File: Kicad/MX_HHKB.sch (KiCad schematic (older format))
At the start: 149 parts, among them J1 USB_mini_micro_B, K1 K00, K10 K09, K11 K0A, K12 K0B, K13 K0C, K14 K10, K15 K11, K16 K12, K17 K13, K18 K14, K19 K15, K2 K01, K20 K16, K21 K17, K22 K18, K23 K19, K24 K1A, K25 K1B, K26 K1C, K27 K20, K28 K21, K29 K22, K3 K02, K30 K23, K31 K24, K32 K25, K33 K26, K34 K27, K35 K28, K36 K29, K37 K2A, K38 K2B, K39 K2C, K4 K03, K40 K30, K41 K31, K42 K32, K43 K33, K44 K34, K45 K35, K46 K36, K47 K37, K48 K38, K49 K39, K5 K04, K50 K3A, K51 K3B, K52 K3C, K53 K41, K54 K42, K55 K45, K56 K48, K57 K49, K58 K4A, K59 K4B, K6 K05, K60 K4C, K61 Ctrl, K62 L_ALT, K63 SPACE, K64 SPACE, K65 R_ALT, K66 R_ALT, K67 R_GUI, K68 R_GUI, K7 K06, K8 K07, K9 K08, SW1 SW_PUSH, U0 ATMEGA32U4, X1 XTAL_GND

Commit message: - Replaced all Diodes with SMD
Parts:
- D1, D10, D11, D12, D13, D14, D15, D16, D17, D18, D19, D2, D20, D21, D22, D23, D24, D25, D26, D27, D28, D29, D3, D30, D31, D32, D33, D34, D35, D36, D37, D38, D39, D4, D40, D41, D42, D43, D44, D45, D46, D47, D48, D49, D5, D50, D51, D52, D53, D54, D55, D56, D57, D58, D59, D6, D60, D7, D8, D9: footprint Footprint:D_SOD123_axial -> Footprint:D_SOD123

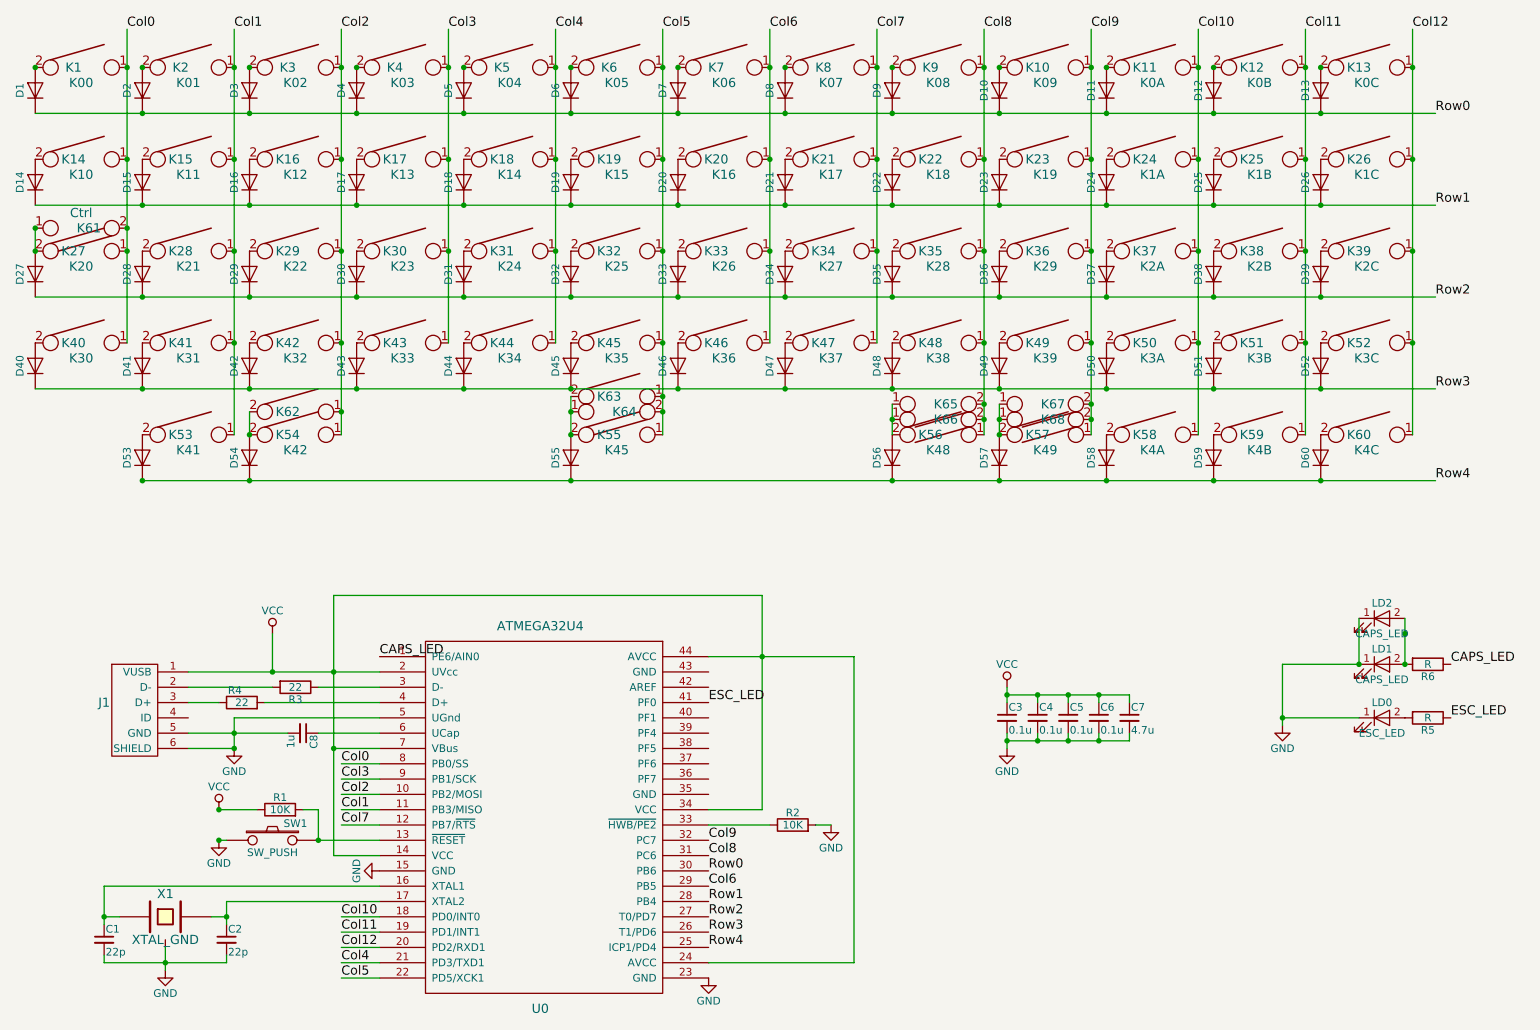
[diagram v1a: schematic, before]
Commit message: - Routing, again and again - Naming all Diodes - Fixed some bugs for holes - Added holes for PCB stabilizers
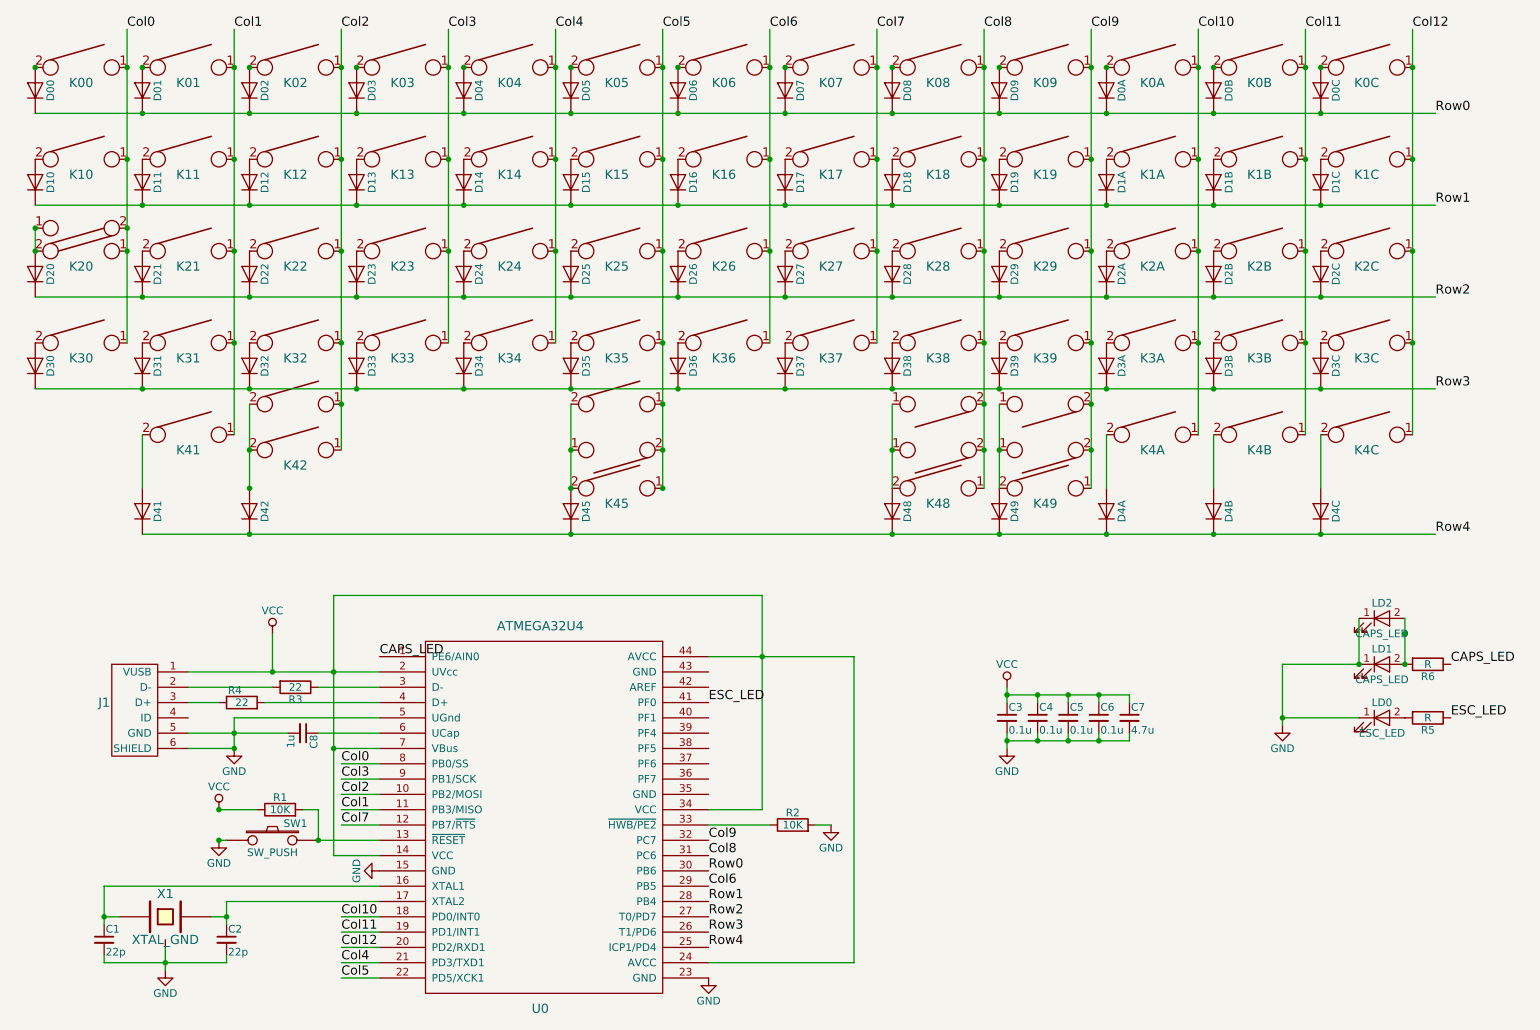
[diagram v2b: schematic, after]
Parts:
- D1: value D -> D00
- D10: value D -> D09
- D11: value D -> D0A
- D12: value D -> D0B
- D13: value D -> D0C
- D14: value D -> D10
- D15: value D -> D11
- D16: value D -> D12
- D17: value D -> D13
- D18: value D -> D14
- D19: value D -> D15
- D2: value D -> D01
- D20: value D -> D16
- D21: value D -> D17
- D22: value D -> D18
- D23: value D -> D19
- D24: value D -> D1A
- D25: value D -> D1B
- D26: value D -> D1C
- D27: value D -> D20
- D28: value D -> D21
- D29: value D -> D22
- D3: value D -> D02
- D30: value D -> D23
- D31: value D -> D24
- D32: value D -> D25
- D33: value D -> D26
- D34: value D -> D27
- D35: value D -> D28
- D36: value D -> D29
- D37: value D -> D2A
- D38: value D -> D2B
- D39: value D -> D2C
- D4: value D -> D03
- D40: value D -> D30
- D41: value D -> D31
- D42: value D -> D32
- D43: value D -> D33
- D44: value D -> D34
- D45: value D -> D35
- D46: value D -> D36
- D47: value D -> D37
- D48: value D -> D38
- D49: value D -> D39
- D5: value D -> D04
- D50: value D -> D3A
- D51: value D -> D3B
- D52: value D -> D3C
- D53: value D -> D41
- D54: value D -> D42
- D55: value D -> D45
- D56: value D -> D48
- D57: value D -> D49
- D58: value D -> D4A
- D59: value D -> D4B
- D6: value D -> D05
- D60: value D -> D4C
- D7: value D -> D06
- D8: value D -> D07
- D9: value D -> D08

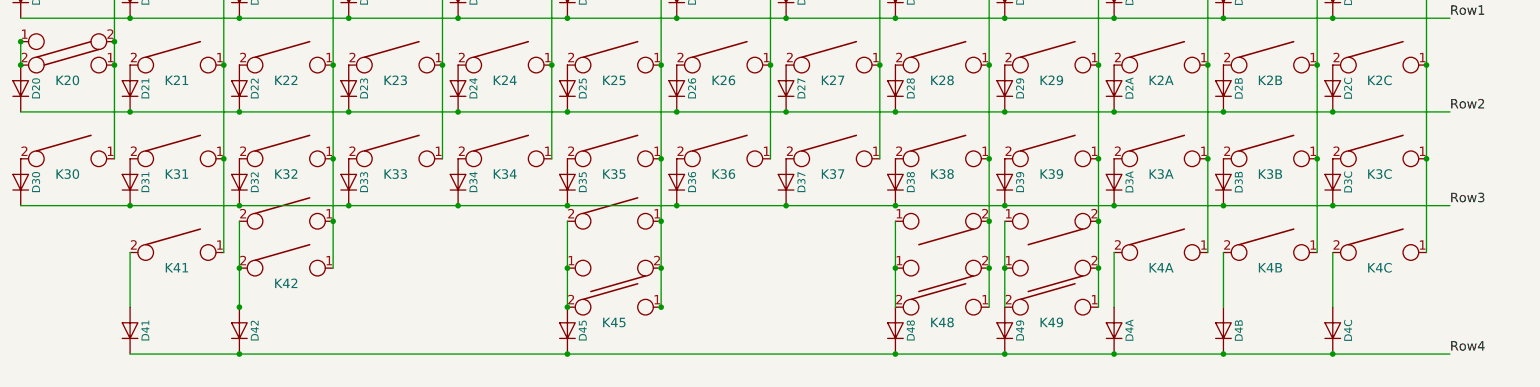
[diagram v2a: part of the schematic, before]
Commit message: - Updated plate.dxf (now use layers to simulate all available layouts) - Added revert 6u spacebar
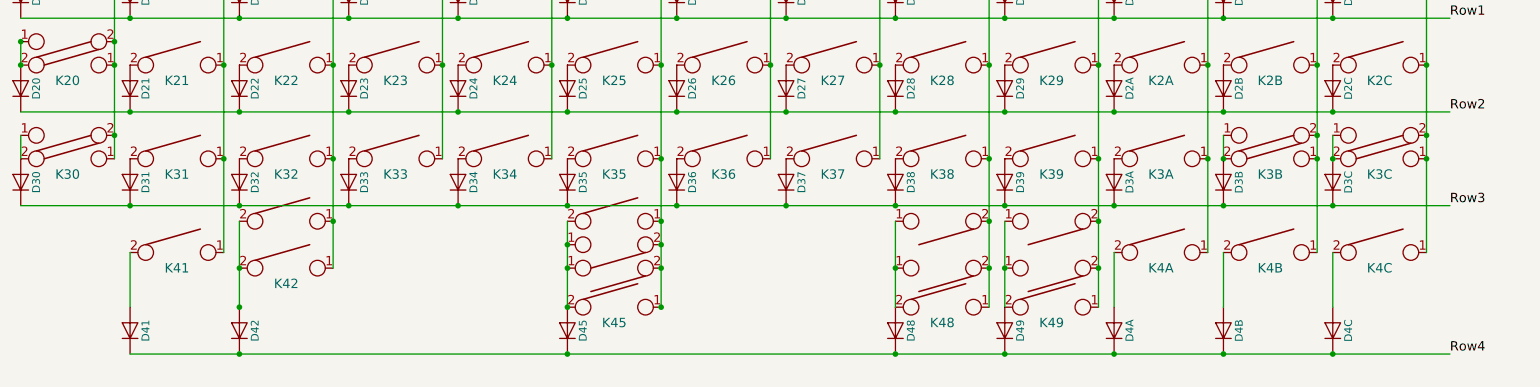
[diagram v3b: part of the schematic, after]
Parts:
- added K69: K30, Footprint:Mx_Alps_225, symbol KEYSW
- added K70: K3C, Footprint:Mx_Alps_100, symbol KEYSW
- added K71: K3B, Footprint:Mx_Alps_175, symbol KEYSW
- added K72: SPACE, Footprint:Mx_Alps_100, symbol KEYSW
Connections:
- net Col0: now also K69.2
- net Col11: now also K71.2
- net Col12: now also K70.2
- net Col5: now also K72.2
- net at D55.2 (A), K55.2, K63.2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: now also K72.1
- net at D40.2 (A), K40.2: now also K69.1
- net at D51.2 (A), K51.2: now also K71.1
- net at D52.2 (A), K52.2: now also K70.1
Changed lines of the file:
@@
 Connection ~ 2150 4150
 Connection ~ 4250 4150
+$Comp
+L KEYSW K69
+U 1 1 591EE9FF
+P 1050 2750
+F 0 "K69" H 1000 2750 60  0001 C CNN
+F 1 "K30" H 1050 2650 60  0001 C CNN
+F 2 "Footprint:Mx_Alps_225" H 1050 2750 60  0001 C CNN
+F 3 "" H 1050 2750 60  0000 C CNN
+	1    1050 2750
+	-1   0    0    1
+$EndComp
+Wire Wire Line
+	750  2750 750  2900
+Connection ~ 1350 2750
+$Comp
+L KEYSW K70
+U 1 1 59228C81
+P 9450 2750
+F 0 "K70" H 9400 2750 60  0001 C CNN
+F 1 "K3C" H 9450 2650 60  0001 C CNN
+F 2 "Footprint:Mx_Alps_100" H 9450 2750 60  0001 C CNN
+F 3 "" H 9450 2750 60  0000 C CNN
+	1    9450 2750
+	-1   0    0    1
+$EndComp
+Wire Wire Line
+	9150 2750 9150 2900
+Connection ~ 9150 2900
+Connection ~ 9750 2750
+$Comp
+L KEYSW K71
+U 1 1 59228EDE
+P 8750 2750
+F 0 "K71" H 8700 2750 60  0001 C CNN
+F 1 "K3B" H 8750 2650 60  0001 C CNN
+F 2 "Footprint:Mx_Alps_175" H 8750 2750 60  0001 C CNN
+F 3 "" H 8750 2750 60  0000 C CNN
+	1    8750 2750
+	-1   0    0    1
+$EndComp
+Wire Wire Line
+	8450 2750 8450 2900
+Connection ~ 8450 2900
+Connection ~ 9050 2750
+$Comp
+L KEYSW K72
+U 1 1 5924807F
+P 4550 3450
+F 0 "K72" H 4500 3450 60  0001 C CNN
+F 1 "SPACE" H 4550 3350 60  0001 C CNN
+F 2 "Footprint:Mx_Alps_100" H 4550 3450 60  0001 C CNN
+F 3 "" H 4550 3450 60  0000 C CNN
+	1    4550 3450
+	-1   0    0    1
+$EndComp
+Connection ~ 4250 3450
+Connection ~ 4850 3450
 $EndSCHEMATC
